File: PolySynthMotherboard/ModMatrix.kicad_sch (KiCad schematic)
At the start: 84 parts, among them SW501 MD1, SW502 MD2, SW503 MD3, SW504 MD4, SW505 MD5, SW506 MD6, SW507 MD7, SW508 MD8, SW509 MS1, SW510 MS2, SW511 MS3, SW512 MS4, SW513 MS5, SW514 MS6, U501 MCP23S17_SS

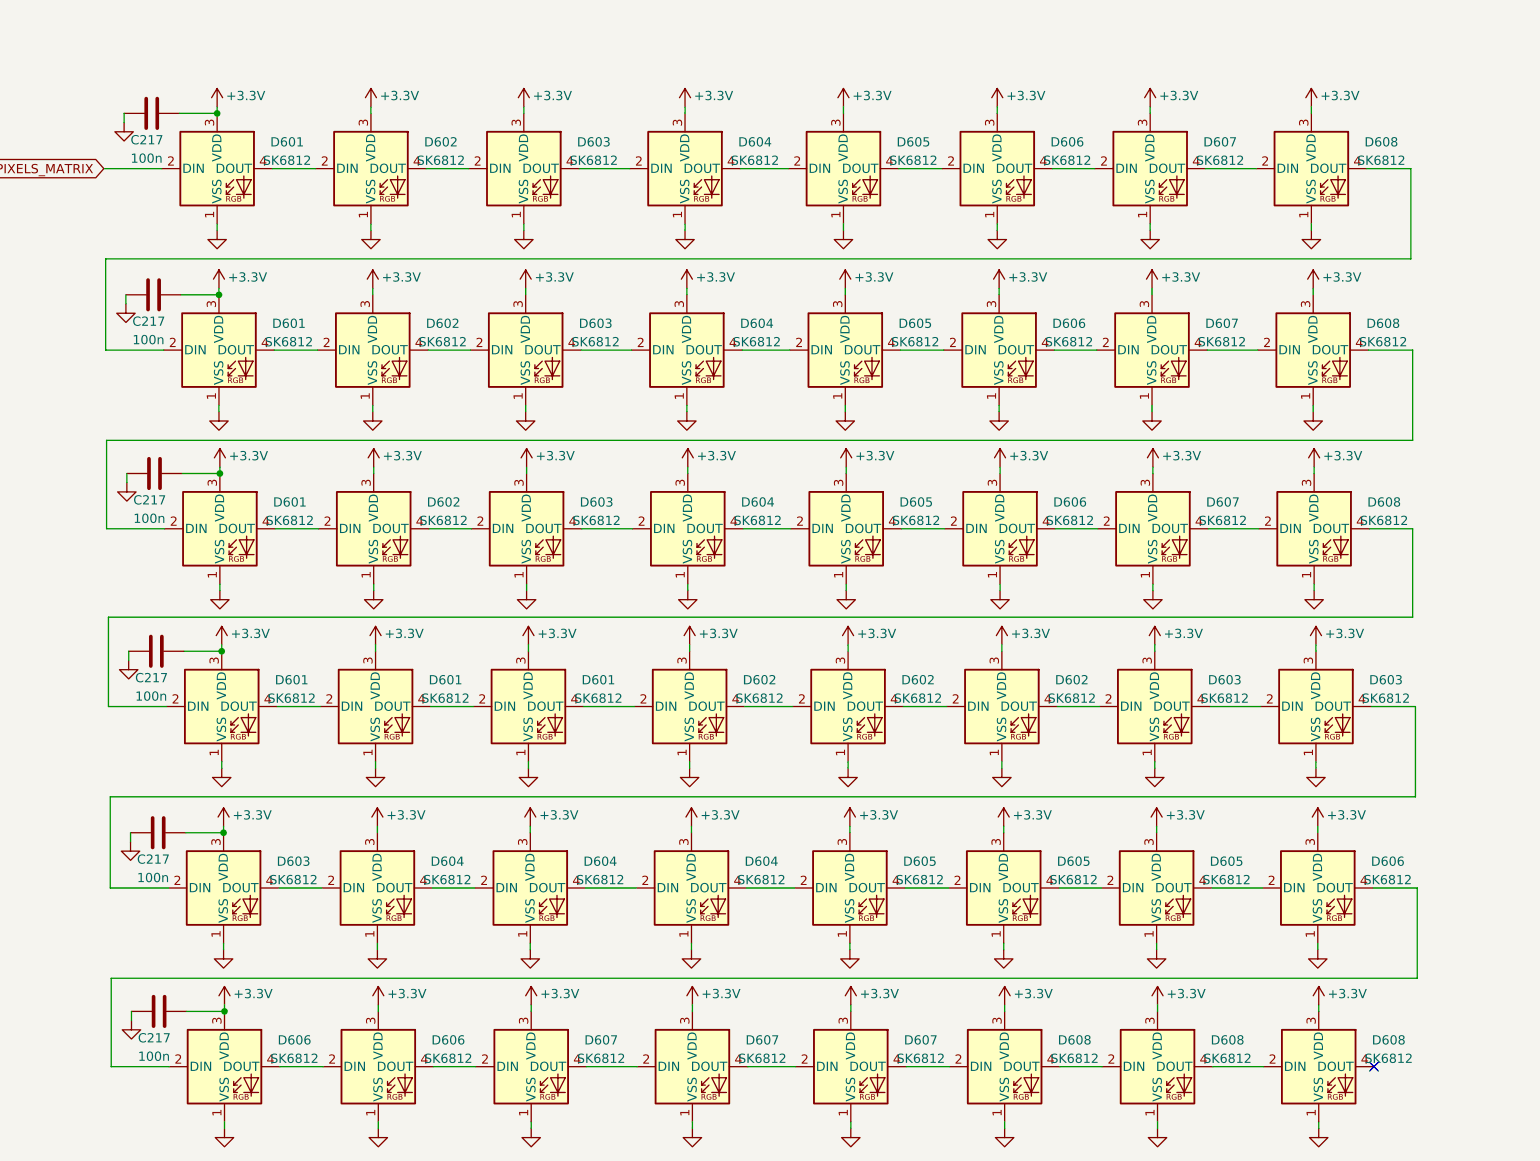
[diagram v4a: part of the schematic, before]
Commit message: updated to kicad 8
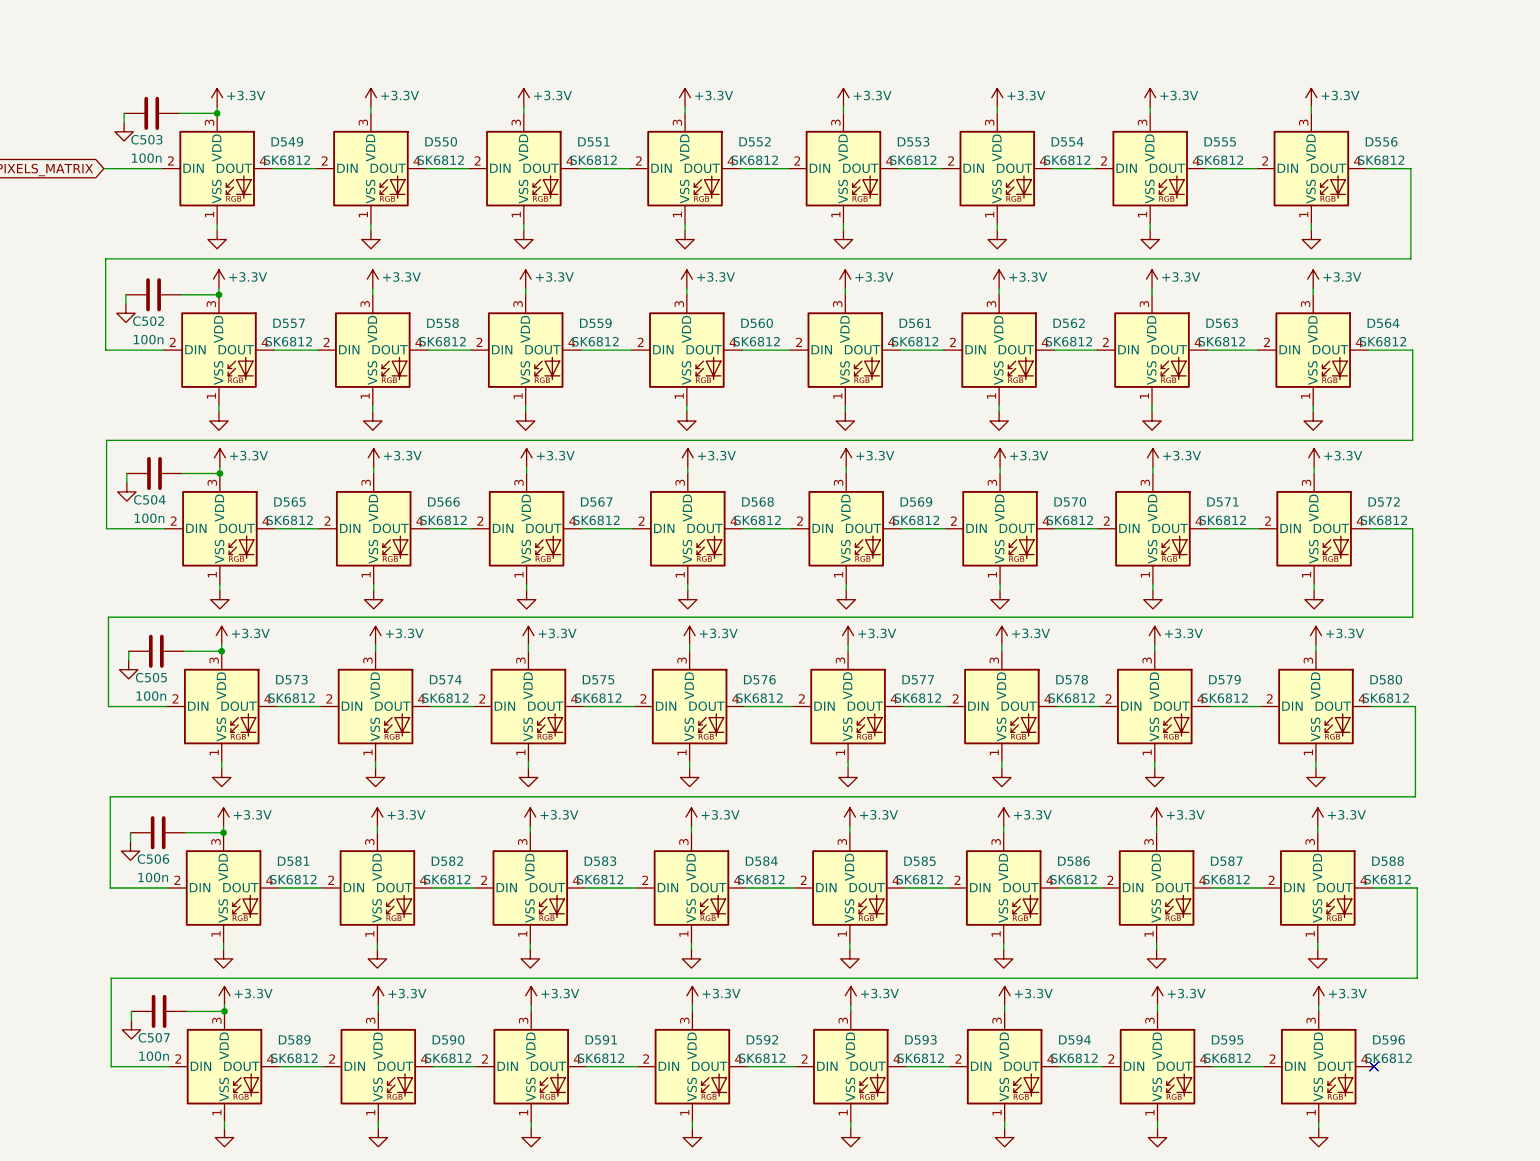
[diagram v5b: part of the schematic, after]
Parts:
- renumbered C217 to C502, C217 to C503, C217 to C504, C217 to C505, C217 to C506, C217 to C507, D601 to D549, D602 to D550, D603 to D551, D604 to D552, D605 to D553, D606 to D554, D607 to D555, D608 to D556, D601 to D557, D602 to D558, D603 to D559, D604 to D560, D605 to D561, D606 to D562, D607 to D563, D608 to D564, D601 to D565, D602 to D566, D603 to D567, D604 to D568, D605 to D569, D606 to D570, D607 to D571, D608 to D572, D601 to D573, D601 to D574, D601 to D575, D602 to D576, D602 to D577, D602 to D578, D603 to D579, D603 to D580, D603 to D581, D604 to D582, D604 to D583, D604 to D584, D605 to D585, D605 to D586, D605 to D587, D606 to D588, D606 to D589, D606 to D590, D607 to D591, D607 to D592, D607 to D593, D608 to D594, D608 to D595, D608 to D596

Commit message: fixed footprints, switched optocoupler
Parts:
- R501, R502, R503, R504, R505, R506, R507, R508, R509, R510, R511, R512, R513, R514: footprint PCM_Resistor_SMD_AKL:R_0805_2012Metric -> Resistor_SMD:R_0805_2012Metric
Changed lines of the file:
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@@
 			)
 		)
-		(property "Footprint" "PCM_Resistor_SMD_AKL:R_0805_2012Metric"
+		(property "Footprint" "Resistor_SMD:R_0805_2012Metric"
 			(at 175.006 69.088 90)
 			(effects
@@
 			)
 		)
-		(property "Footprint" "PCM_Resistor_SMD_AKL:R_0805_2012Metric"
+		(property "Footprint" "Resistor_SMD:R_0805_2012Metric"
 			(at 156.591 69.469 90)
 			(effects
@@
 			)
 		)
-		(property "Footprint" "PCM_Resistor_SMD_AKL:R_0805_2012Metric"
+		(property "Footprint" "Resistor_SMD:R_0805_2012Metric"
 			(at 139.7 69.596 90)
 			(effects
@@
 			)
 		)
-		(property "Footprint" "PCM_Resistor_SMD_AKL:R_0805_2012Metric"
+		(property "Footprint" "Resistor_SMD:R_0805_2012Metric"
 			(at 140.081 35.814 90)
 			(effects
@@
 			)
 		)
-		(property "Footprint" "PCM_Resistor_SMD_AKL:R_0805_2012Metric"
+		(property "Footprint" "Resistor_SMD:R_0805_2012Metric"
 			(at 156.972 35.687 90)
 			(effects
@@
 			)
 		)
-		(property "Footprint" "PCM_Resistor_SMD_AKL:R_0805_2012Metric"
+		(property "Footprint" "Resistor_SMD:R_0805_2012Metric"
 			(at 121.158 69.469 90)
 			(effects
@@
 			)
 		)
-		(property "Footprint" "PCM_Resistor_SMD_AKL:R_0805_2012Metric"
+		(property "Footprint" "Resistor_SMD:R_0805_2012Metric"
 			(at 121.539 35.687 90)
 			(effects
@@
 			)
 		)
-		(property "Footprint" "PCM_Resistor_SMD_AKL:R_0805_2012Metric"
+		(property "Footprint" "Resistor_SMD:R_0805_2012Metric"
 			(at 194.056 35.56 90)
 			(effects
@@
 			)
 		)
-		(property "Footprint" "PCM_Resistor_SMD_AKL:R_0805_2012Metric"
+		(property "Footprint" "Resistor_SMD:R_0805_2012Metric"
 			(at 102.489 69.215 90)
 			(effects
@@
 			)
 		)
-		(property "Footprint" "PCM_Resistor_SMD_AKL:R_0805_2012Metric"
+		(property "Footprint" "Resistor_SMD:R_0805_2012Metric"
 			(at 102.87 35.433 90)
 			(effects
@@
 			)
 		)
-		(property "Footprint" "PCM_Resistor_SMD_AKL:R_0805_2012Metric"
+		(property "Footprint" "Resistor_SMD:R_0805_2012Metric"
 			(at 212.598 35.687 90)
 			(effects
@@
 			)
 		)
-		(property "Footprint" "PCM_Resistor_SMD_AKL:R_0805_2012Metric"
+		(property "Footprint" "Resistor_SMD:R_0805_2012Metric"
 			(at 175.387 35.306 90)
 			(effects
@@
 			)
 		)
-		(property "Footprint" "PCM_Resistor_SMD_AKL:R_0805_2012Metric"
+		(property "Footprint" "Resistor_SMD:R_0805_2012Metric"
 			(at 229.489 35.56 90)
 			(effects
@@
 			)
 		)
-		(property "Footprint" "PCM_Resistor_SMD_AKL:R_0805_2012Metric"
+		(property "Footprint" "Resistor_SMD:R_0805_2012Metric"
 			(at 193.675 69.342 90)
 			(effects

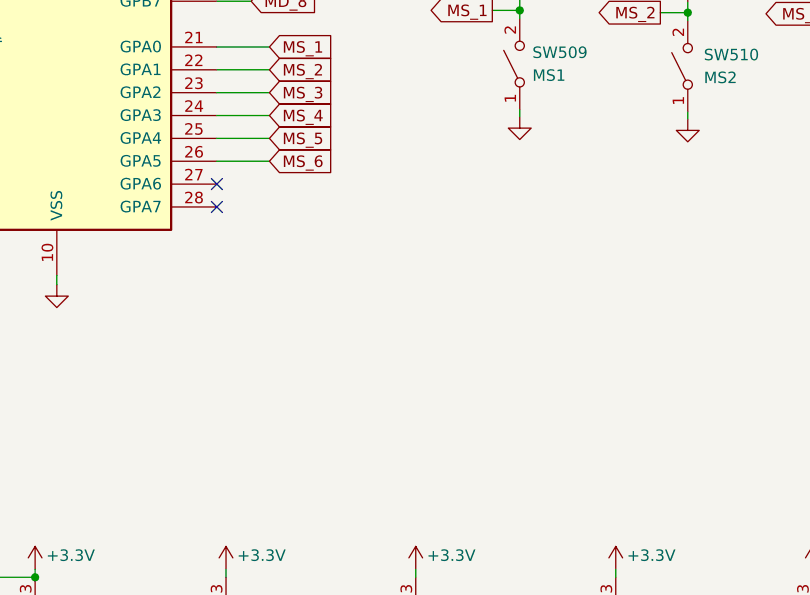
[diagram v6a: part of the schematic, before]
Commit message: separate power supply board
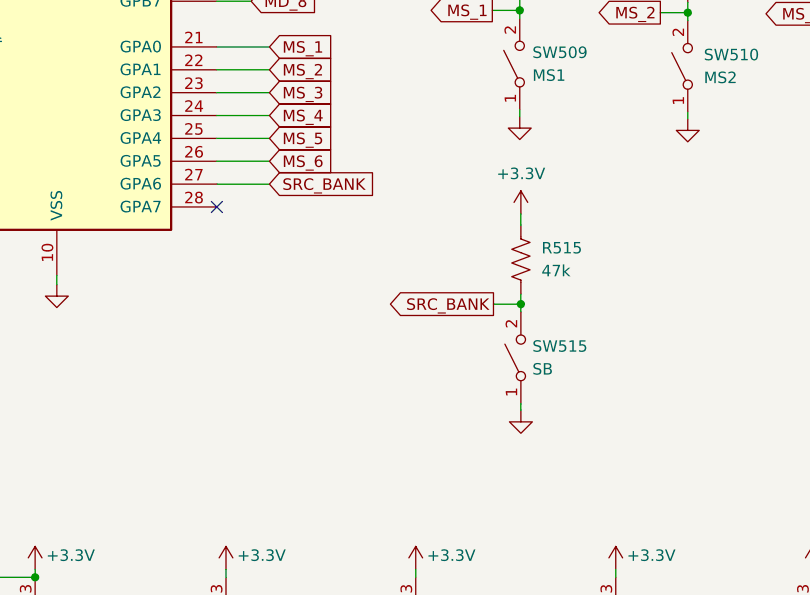
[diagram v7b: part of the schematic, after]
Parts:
- added R515: 47k, Resistor_SMD:R_0805_2012Metric, symbol Device:R_US
- added SW515: SB, Button_Switch_THT:SW_PUSH_6mm, symbol Switch:SW_SPST
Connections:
- net +3.3V: now also R515.1
- net GND: now also SW515.1 (A)
- net SRC_BANK: now reaches U501.27 (GPA6)
- net SRC_BANK: now also R515.2, SW515.2 (B)
- no-connect marks 5 -> 4

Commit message: board iteration
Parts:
- added R516: 22R, Resistor_SMD:R_0805_2012Metric, symbol Device:R_US
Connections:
- net EXP_MISO: now also R516.1; no longer U501.14 (SO)
- new net: R516.2, U501.14 (SO)
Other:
- moved on the sheet: C501, C502, C503, C504, C505, C506, C507, D549, D550, D551, D552, D553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
